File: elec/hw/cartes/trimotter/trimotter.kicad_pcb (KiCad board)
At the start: 2 copper layers, 60 x 47 mm, 68 parts, among them J2 22053051, J3 2-1445055-2, J4 2-1445055-3, J5 3-794630-6, J6 3-794630-4, Q1 2N7002, U1 DRV8243HQDGQRQ1, U2 SN74LVC2T45DCU, U4 PCA9535PW

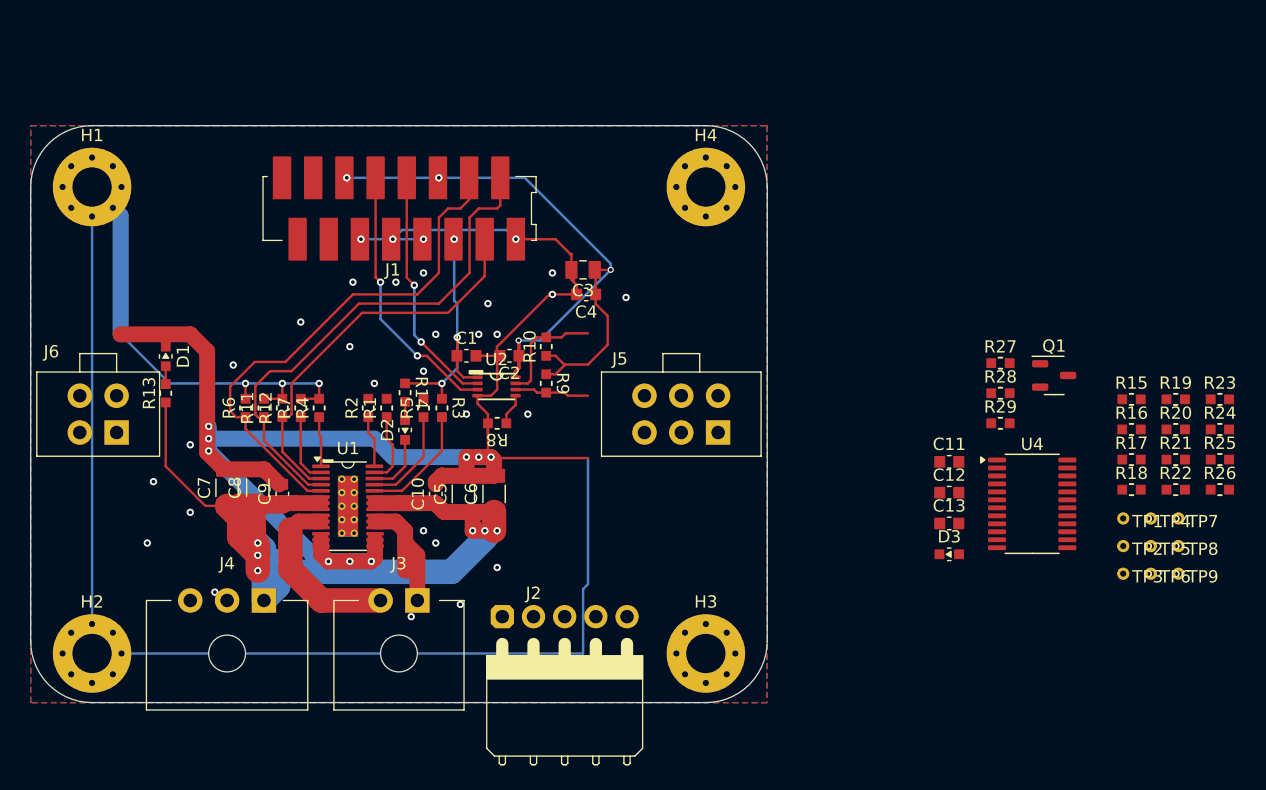
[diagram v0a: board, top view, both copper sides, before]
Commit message: trimotter schematic corrected after review. component placement done, routing tbd
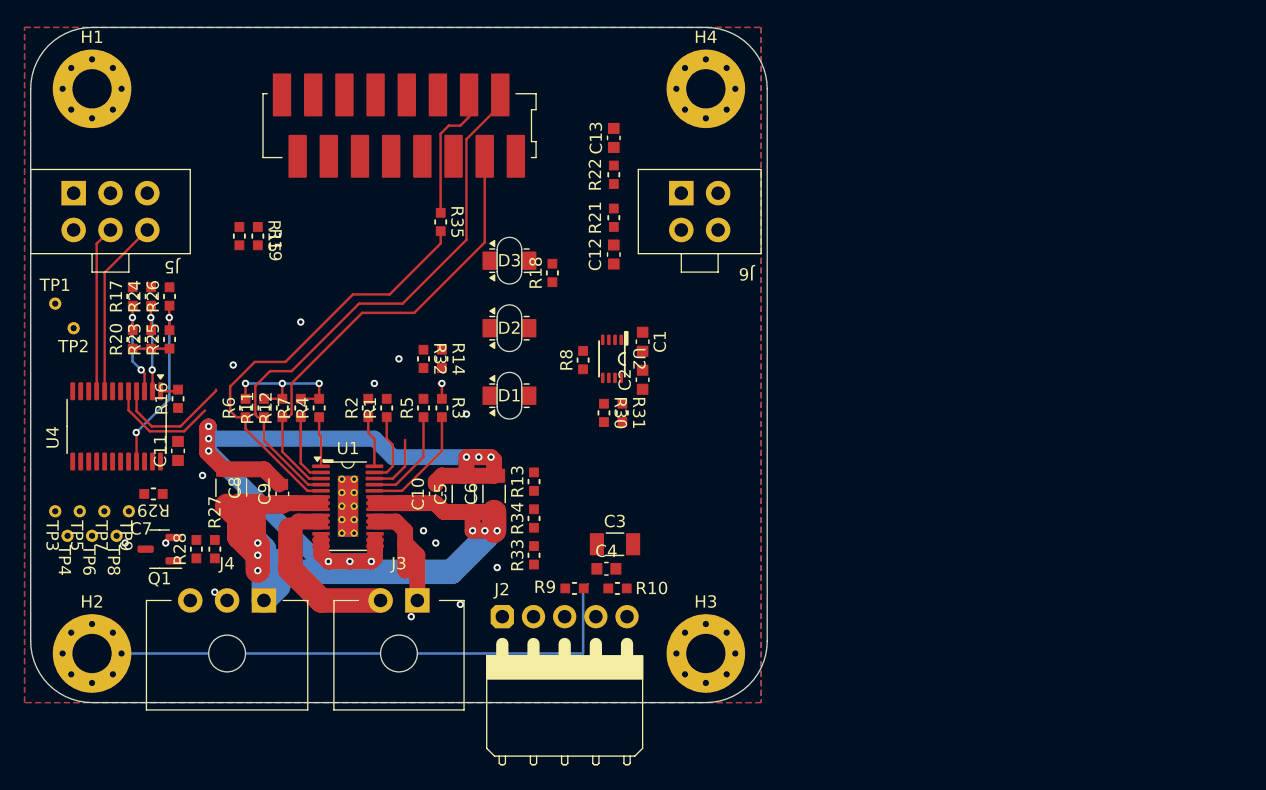
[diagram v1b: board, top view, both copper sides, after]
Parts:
- added R30: 0R, cocotter_resistor:r0603_reflow, F.Cu at (116.7, 146.4)
- added R31: 0R, cocotter_resistor:r0603_reflow, F.Cu at (118.2, 146.4)
- added R32: 1k 1%, cocotter_resistor:r0603_reflow, F.Cu at (102.0, 142.0)
- added R33: 3k3 1%, cocotter_resistor:r0603_reflow, F.Cu at (111.0, 158.0)
- added R34: 3k3 1%, cocotter_resistor:r0603_reflow, F.Cu at (111.0, 155.0)
- added R35: 0R, cocotter_resistor:r0603_reflow, F.Cu at (103.4, 130.8)
- C3: value 1µF 50V -> 47µF 10V; footprint cocotter_capacitors:C_0805_2012Metric -> cocotter_capacitors:C_1206_3216Metric
- D1, D3: value green, 0603 -> green, 1206; footprint cocotter_diodes:LED_0603_1608Metric -> cocotter_diodes:24-21-1206_reverse_mount
- D2: value yellow, 0603 -> red, 1206; footprint cocotter_diodes:LED_0603_1608Metric -> cocotter_diodes:24-21-1206_reverse_mount
- R13: value 10k 1% -> 3k3 1%
- R14: value 470R 1% -> 1k 1%
- moved TP1 88.7 mm to (72.0, 137.5)
- moved TP4 88.3 mm to (73.0, 156.4), turned to -90 degrees
- moved R24 87.7 mm to (79.8, 136.9), turned to 90 degrees
- moved TP7 87.5 mm to (76.0, 154.4), turned to -90 degrees
- moved TP2 87.3 mm to (73.5, 139.5)
- moved TP5 87.3 mm to (74.0, 154.4), turned to -90 degrees
- moved R23 87.2 mm to (79.8, 140.4), turned to 90 degrees
- moved TP3 87.1 mm to (72.0, 154.4), turned to -90 degrees
- moved R26 87.0 mm to (81.3, 136.9), turned to 90 degrees
- moved TP8 86.5 mm to (77.0, 156.4), turned to -90 degrees
- moved TP6 86.3 mm to (75.0, 156.4), turned to -90 degrees
- moved R25 86.1 mm to (81.3, 140.4), turned to 90 degrees
- moved TP9 85.7 mm to (78.0, 154.4), turned to -90 degrees
- moved R20 85.3 mm to (78.3, 140.4), turned to 90 degrees
- moved R17 82.4 mm to (78.3, 136.9), turned to 90 degrees
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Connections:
- J1 pad 4: /brake_mot_3v3 -> Net-(J1-brake_3v3)
- J4 pad 2: unconnected-(J4-Pad2) -> VMOT
- R13 pad 1: VMOT -> Net-(R13-Pad1)
- R14 pad 1: +3V3 -> Net-(D2-PadA)
- R14 pad 2: Net-(D2-PadA) -> +3V3
- TP2 pad 1: Net-(U4-IO1_0) -> Net-(U4-IO0_6)
- TP3 pad 1: Net-(U4-IO1_1) -> Net-(U4-IO1_0)
- TP4 pad 1: Net-(U4-IO1_2) -> Net-(U4-IO1_1)
- TP5 pad 1: Net-(U4-IO1_3) -> Net-(U4-IO1_2)
- TP6 pad 1: Net-(U4-IO1_4) -> Net-(U4-IO1_3)
- TP7 pad 1: Net-(U4-IO1_5) -> Net-(U4-IO1_4)
- TP8 pad 1: Net-(U4-IO1_6) -> Net-(U4-IO1_5)
- TP9 pad 1: Net-(U4-IO1_7) -> Net-(U4-IO1_6)
- U2 pad 6: /encoder_A_5v -> Net-(U2-B2)
- U2 pad 7: /encoder_B_5v -> Net-(U2-B1)
- U4 pad 10: /vmot_absent_3v3 -> Net-(U4-IO0_6)
- U4 pad 20: Net-(U4-IO1_7) -> /vmot_absent_3v3
- U4 pad 4: /nFAULT_3V3 -> /ctc_right_3v3
- U4 pad 5: /brake_mot_3v3 -> /ctc_left_3v3
- U4 pad 6: /ctc_right_3v3 -> /nFAULT_3V3
- U4 pad 7: /ctc_left_3v3 -> /brake_mot_3v3
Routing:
- net GND: track 264.9 -> 128.6 mm, vias 43 -> 26
- net P5V: track 53.3 -> 0.00 mm, vias 4 -> 0
- net /encoder_B_3v3: track 21.9 -> 0.00 mm, vias 2 -> 0
- net /encoder_A_3v3: track 20.7 -> 0.00 mm, vias 2 -> 0
- net +3V3: track 21.6 -> 4.83 mm, vias 3 -> 1
- net Net-(U4-A0): track 0.00 -> 14.9 mm, vias 0 -> 2
- net /reset_tof_3v3: track 0.00 -> 14.6 mm
- net /enable_tof_3v3: track 0.00 -> 13.6 mm
- net VMOT: track 91.5 -> 80.0 mm
- net Net-(J1-brake_3v3): track 0.00 -> 11.1 mm
- net /ctc_right_3v3: track 0.00 -> 9.91 mm
- net /encoder_B_5v: track 9.35 -> 0.00 mm
- net /ctc_left_3v3: track 0.00 -> 9.18 mm
- net Net-(U4-A2): track 0.00 -> 8.38 mm, vias 0 -> 2
- net Net-(U4-A1): track 0.00 -> 8.07 mm, vias 0 -> 2
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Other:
- board size 60 x 47 mm -> 60 x 55 mm

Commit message: trimotter routing ready to review
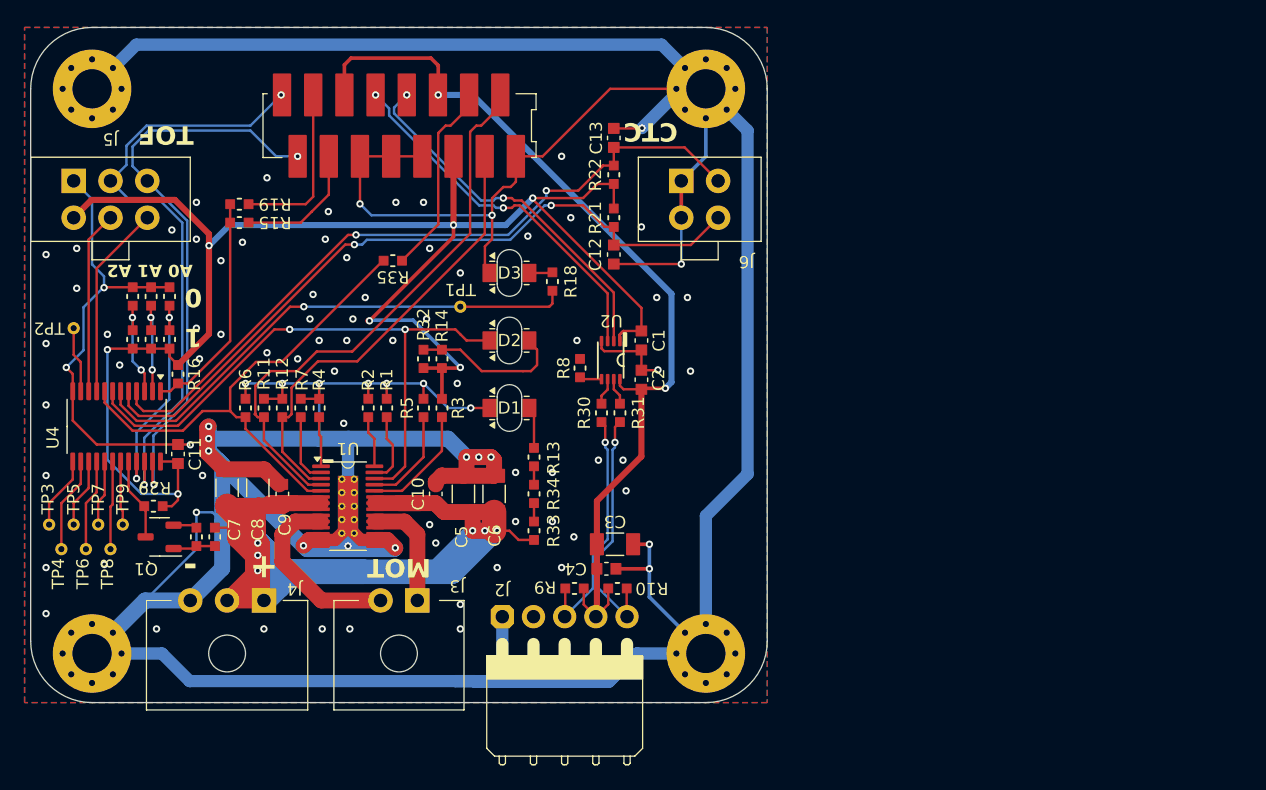
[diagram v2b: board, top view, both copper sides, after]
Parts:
- moved TP1 33.0 mm to (105.0, 137.8)
- moved R35 5.01 mm to (99.5, 134.0), turned to 180 degrees
- moved R19 2.60 mm to (87.0, 129.4), turned to 180 degrees
- moved R13 2.00 mm to (111.0, 150.0)
- moved R16 2.00 mm to (82.0, 143.2), turned to -90 degrees
- moved R33 2.00 mm to (111.0, 156.0)
- moved R34 2.00 mm to (111.0, 153.0)
- moved R15 1.86 mm to (87.0, 130.9), turned to 180 degrees
- moved TP3 1.19 mm to (71.5, 155.5)
- moved TP4 1.19 mm to (72.5, 157.5)
- moved TP5 1.19 mm to (73.5, 155.5)
- moved TP6 1.19 mm to (74.5, 157.5)
- moved TP7 1.19 mm to (75.5, 155.5)
- moved TP8 1.19 mm to (76.5, 157.5)
- moved TP9 1.19 mm to (77.5, 155.5)
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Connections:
- TP2 pad 1: Net-(U4-IO0_6) -> Net-(U4-IO0_7)
- U4 pad 10: Net-(U4-IO0_6) -> /enable_tof_3v3
- U4 pad 11: /led_com_3v3 -> Net-(U4-IO0_7)
- U4 pad 4: /ctc_right_3v3 -> /ctc_left_3v3
- U4 pad 5: /ctc_left_3v3 -> /ctc_right_3v3
- U4 pad 6: /nFAULT_3V3 -> /led_com_3v3
- U4 pad 7: /brake_mot_3v3 -> /nFAULT_3V3
- U4 pad 8: /reset_tof_3v3 -> /brake_mot_3v3
- U4 pad 9: /enable_tof_3v3 -> /reset_tof_3v3
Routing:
- net GND: track 128.6 -> 469.0 mm, vias 26 -> 94
- net +3V3: track 4.83 -> 139.2 mm, vias 1 -> 7
- net P5V: track 0.00 -> 82.4 mm, vias 0 -> 2
- net /ctc_left_3v3: track 9.18 -> 59.9 mm, vias 0 -> 2
- net /ctc_right_3v3: track 9.91 -> 59.8 mm, vias 0 -> 2
- net /scl_tof_3v3: track 0.00 -> 49.5 mm, vias 0 -> 2
- net /sda_tof_3v3: track 0.00 -> 47.5 mm, vias 0 -> 2
- net /nFAULT_3V3: track 5.06 -> 50.3 mm, vias 0 -> 2
- net /led_com_3v3: track 0.00 -> 41.8 mm, vias 0 -> 1
- net VMOT: track 80.0 -> 116.1 mm
- net /encoder_A_3v3: track 0.00 -> 30.0 mm, vias 0 -> 2
- net /encoder_B_3v3: track 0.00 -> 30.0 mm, vias 0 -> 2
- net /encoder_B_5v: track 0.00 -> 19.9 mm, vias 0 -> 1
- net /encoder_A_5v: track 0.00 -> 19.8 mm, vias 0 -> 1
- net Net-(U4-~{INT}): track 1.48 -> 18.5 mm
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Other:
- board text added: "+"
- board text added: "-"
- board text added: "0"
- board text added: "1"
- board text added: "A0 A1 A2"
- board text added: "CTC"
- board text added: "MOT"
- board text added: "TOF"

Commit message: board name added
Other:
- board text added: "TRIM'OTTER 2026"
